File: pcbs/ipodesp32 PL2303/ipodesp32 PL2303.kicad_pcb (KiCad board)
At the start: 2 copper layers, 57.2 x 63 mm, 19 parts, among them IC1 PL2303SA__LF, IC2 3678, J1 USB_A, J2 Conn_01x19_Pin, U1 ESP32-DevKitC

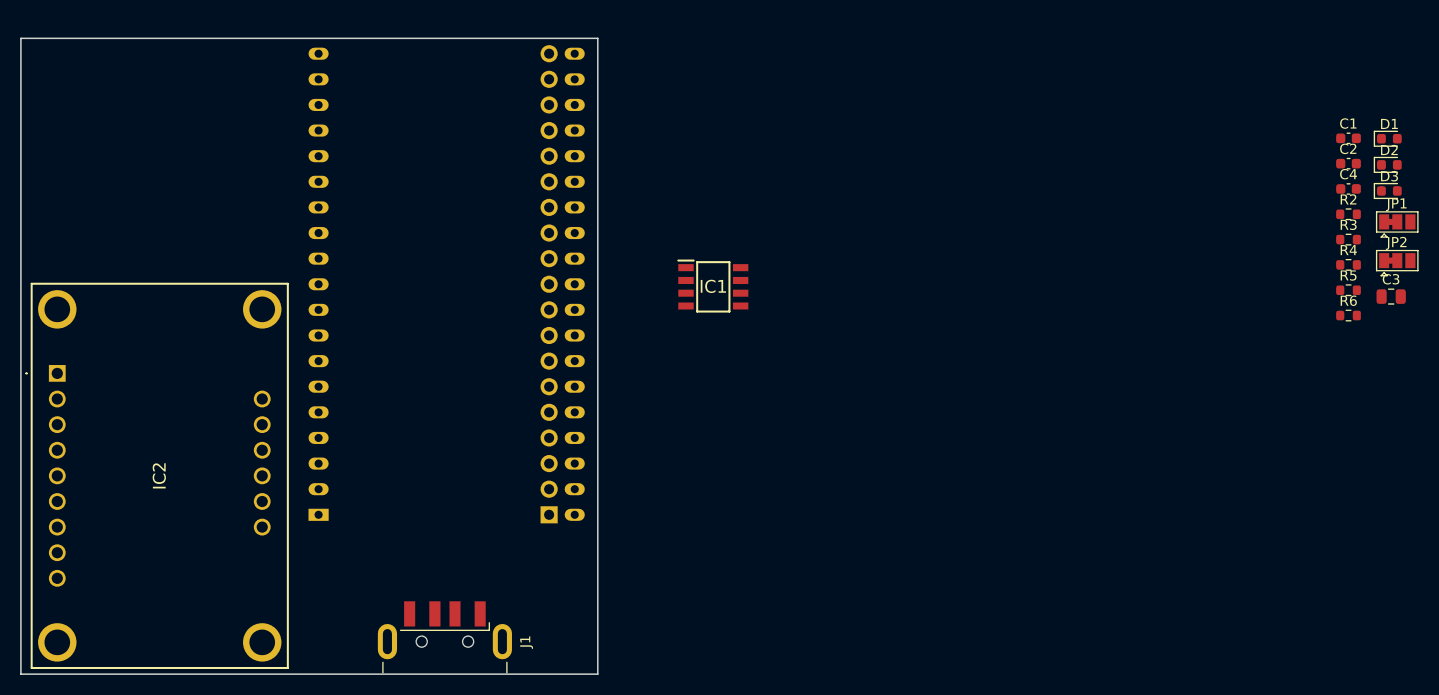
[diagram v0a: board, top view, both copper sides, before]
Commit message: Layout tracing
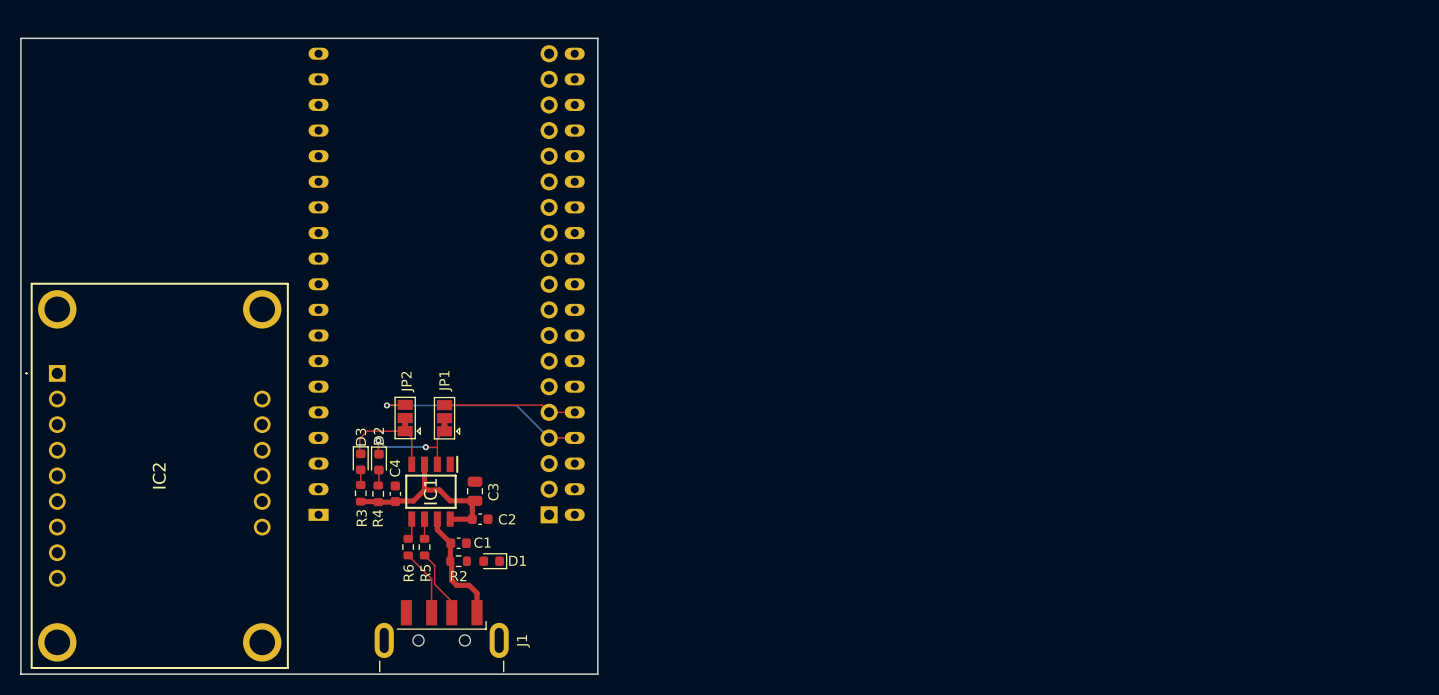
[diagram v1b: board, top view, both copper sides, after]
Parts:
- moved D3 105.5 mm to (132.6, 106.5), turned to -90 degrees
- moved D2 104.4 mm to (134.4, 106.5), turned to -90 degrees
- moved R3 101.1 mm to (132.6, 109.6), turned to -90 degrees
- moved JP2 99.6 mm to (137.0, 102.1), turned to 90 degrees
- moved C4 99.2 mm to (136.1, 109.7), turned to 90 degrees
- moved R4 98.9 mm to (134.4, 109.7), turned to -90 degrees
- moved D1 98.4 mm to (145.6, 116.3), turned to 180 degrees
- moved C1 96.9 mm to (142.3, 114.6)
- moved JP1 96.5 mm to (140.9, 102.2), turned to 90 degrees
- moved R6 96.0 mm to (137.3, 114.9), turned to -90 degrees
- moved R5 95.1 mm to (139.0, 114.9), turned to -90 degrees
- moved R2 94.7 mm to (142.3, 116.3), turned to 180 degrees
- moved C2 93.0 mm to (144.5, 112.2)
- moved C3 92.9 mm to (144.0, 109.4), turned to 90 degrees
- moved IC1 34.6 mm to (139.6, 109.4), turned to -90 degrees
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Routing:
- net TX0: track 0.00 -> 21.8 mm, vias 0 -> 1
- net +3V3: track 0.00 -> 19.0 mm
- net RX0: track 0.00 -> 13.2 mm
- net +5V: track 0.00 -> 11.7 mm
- net TXD: track 0.00 -> 11.1 mm, vias 0 -> 2
- net RXD: track 0.00 -> 9.94 mm
- net Net-(J1-D-): track 0.00 -> 6.80 mm
- net Net-(J1-D+): track 0.00 -> 6.64 mm
- net Net-(IC1-DP): track 0.00 -> 2.10 mm
- net Net-(IC1-DM): track 0.00 -> 1.96 mm
- net Net-(D2-A): track 0.00 -> 1.57 mm
- net Net-(D3-A): track 0.00 -> 1.51 mm

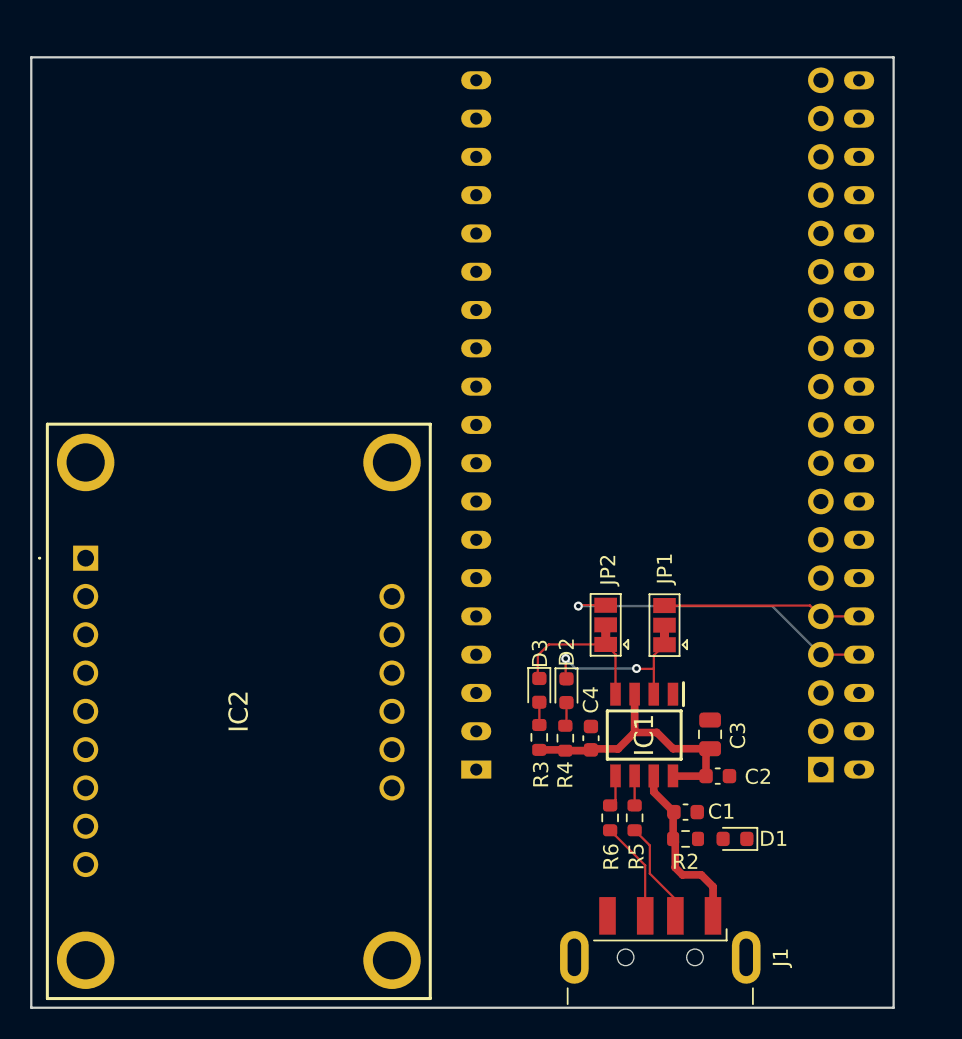
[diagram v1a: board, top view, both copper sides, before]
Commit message: Update to PCB with integrated PL2303
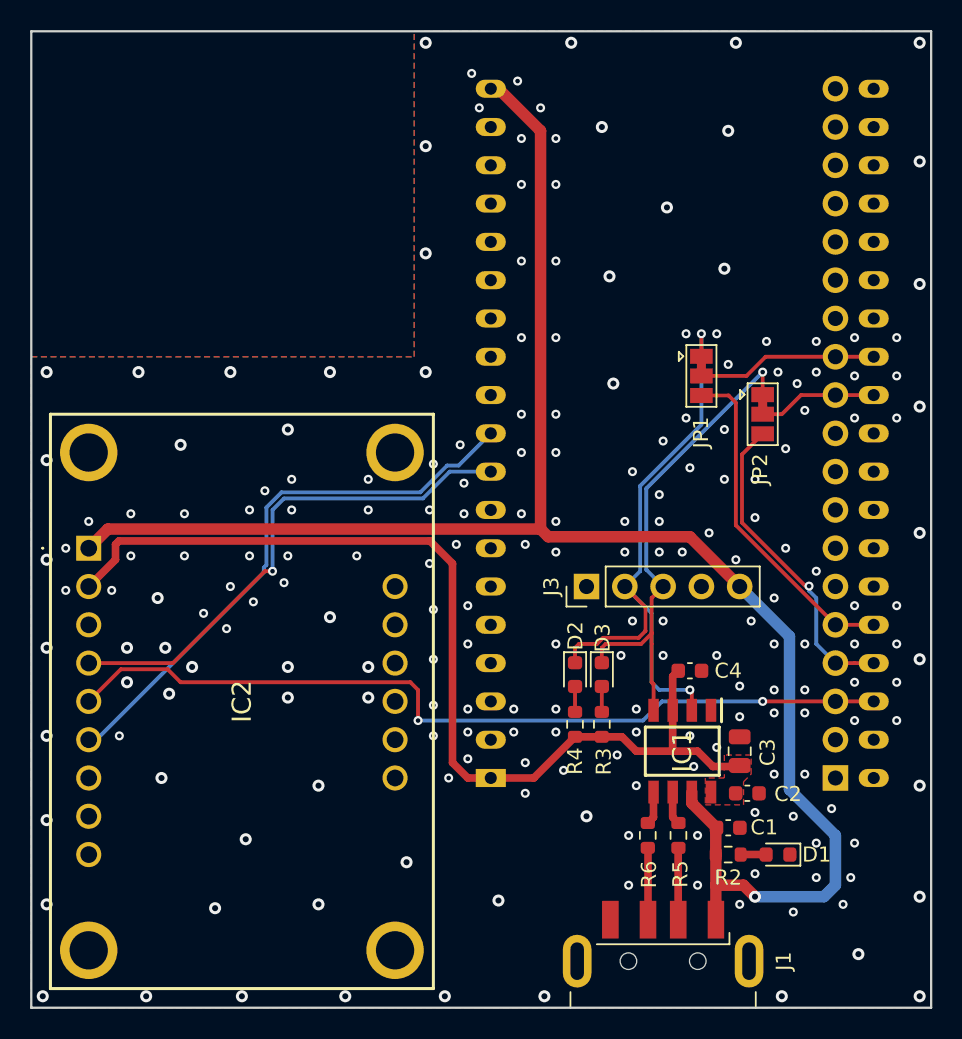
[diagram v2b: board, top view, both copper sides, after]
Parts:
- added J3: Conn_01x05_Pin, Connector_PinHeader_2.54mm:PinHeader_1x05_P2.54mm_Vertical, F.Cu at (135.8, 99.6)
- moved JP2 17.4 mm to (147.5, 88.2), turned to -90 degrees
- moved JP1 16.7 mm to (143.4, 85.6), turned to -90 degrees
- moved C4 7.94 mm to (142.6, 105.2), turned to 0 degrees
- moved D3 4.28 mm to (136.8, 105.4)
- moved R3 4.24 mm to (136.8, 108.7)
- moved R5 3.13 mm to (141.9, 116.1)
- moved D1 3.04 mm to (148.5, 117.4)
- moved C1 3.01 mm to (145.2, 115.6)
- moved R2 3.01 mm to (145.2, 117.4)
- moved R6 2.76 mm to (139.8, 116.1)
- moved IC1 2.74 mm to (142.1, 110.5)
- moved C2 2.27 mm to (146.4, 113.3)
- moved C3 2.26 mm to (145.9, 110.5)
- moved D2 1.21 mm to (135.0, 105.4)
- moved R4 1.12 mm to (135.0, 108.7)
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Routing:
- net +5V: track 11.7 -> 116.3 mm, vias 0 -> 1
- net DIN: track 0.00 -> 56.1 mm, vias 0 -> 2
- net +3V3: track 19.0 -> 66.8 mm
- net BCLK: track 0.00 -> 37.5 mm
- net WSEL: track 0.00 -> 34.3 mm, vias 0 -> 1
- net TXD: track 11.1 -> 41.2 mm
- net RXD: track 9.94 -> 32.7 mm, vias 0 -> 1
- net RX1: track 0.00 -> 12.0 mm
- net RX0: track 13.2 -> 22.5 mm
- net TX1: track 0.00 -> 7.89 mm
- net Net-(J1-D-): track 6.80 -> 4.77 mm
- net Net-(J1-D+): track 6.64 -> 4.77 mm
- net Net-(D1-A): track 0.00 -> 1.69 mm
- net TX0: track 21.8 -> 21.1 mm
- net GND: vias 0 -> 209
- added copper zone on F.Cu, net +3V3
- added copper zone on B.Cu, net GND
- added copper zone on F.Cu, net GND
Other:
- board size 57.2 x 63 mm -> 59.7 x 64.8 mm

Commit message: PCBWay Quote
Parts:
- D1, D2, D3: value 2V -> 2.1V
- IC1: value PL2303SA__LF -> PL2303GS
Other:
- board text added: "${REVISION}"

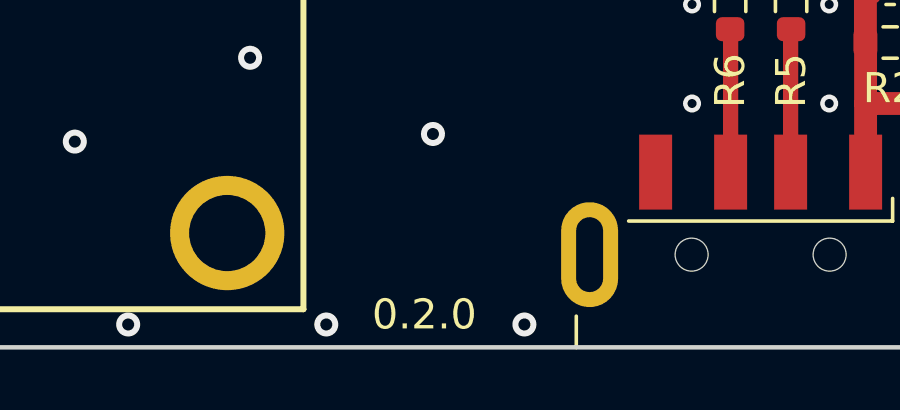
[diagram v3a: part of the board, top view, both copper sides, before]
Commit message: Corrected GS to GL on PL2303
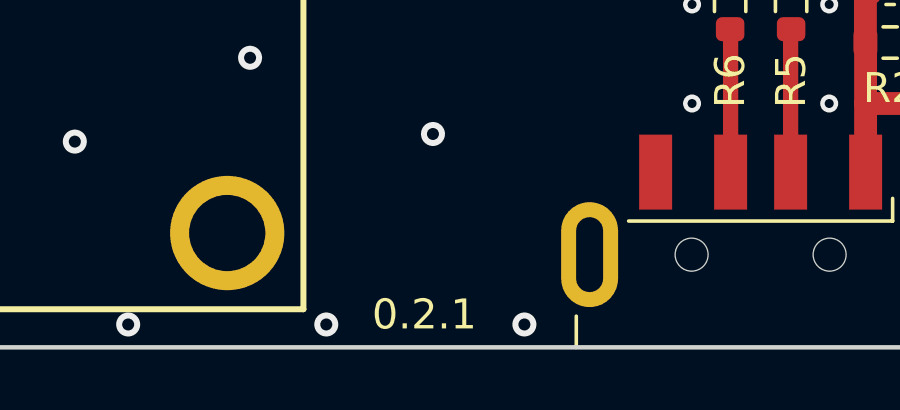
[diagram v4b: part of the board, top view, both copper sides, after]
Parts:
- IC1: value PL2303GS -> PL2303GL
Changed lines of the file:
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@@
   (title_block
     (title "iPod ESP32 barebones PCB")
-    (date "2024-06-04")
-    (rev "0.2.0")
+    (date "2024-07-16")
+    (rev "0.2.1")
     (company "(c) Martin Roger")
   )
@@
         (effects (font (size 1.27 1.27) (thickness 0.254)))
     )
-    (fp_text value "PL2303GS" (at 0 0 90) (layer "F.SilkS") hide
+    (fp_text value "PL2303GL" (at 0 0 90) (layer "F.SilkS") hide
         (effects (font (size 1.27 1.27) (thickness 0.254)))
     )
